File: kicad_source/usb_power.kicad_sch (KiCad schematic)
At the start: 39 parts, among them CN5 USB_C_Receptacle_USB2.0, Q1 2N7002, Q2 2N7002, Q3 BC847, Q4 BC847, Q5 NTR4171P, SW3 SWITCH_INV, U1 TPS383X, U2 MCP73831, U3 TPS736XX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

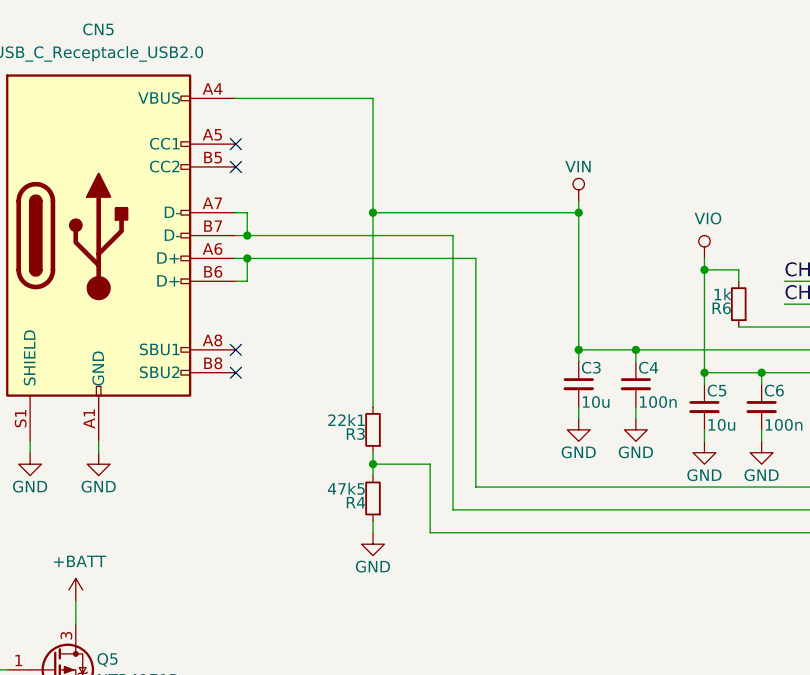
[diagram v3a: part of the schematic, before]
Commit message: added resistors on USB CC
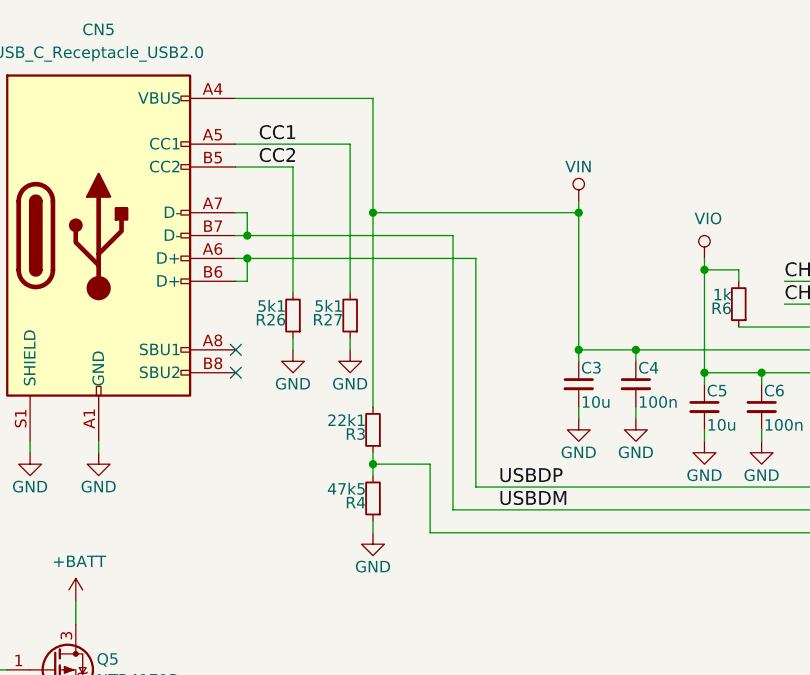
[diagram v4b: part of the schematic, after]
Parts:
- added R26, R27: 5k1, Resistor_SMD:R_0603_1608Metric, symbol Device:R_Small
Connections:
- net GND: now also R26.1, R27.1
- net USBDP: now reaches CN5.A6 (D+), CN5.B6 (D+), U4.4 (D+)
- net USBDM: now reaches CN5.A7 (D-), CN5.B7 (D-), U4.5 (D-)
- net CC1: now reaches CN5.A5 (CC1)
- net CC1: now also R27.2
- net CC2: now reaches CN5.B5 (CC2)
- net CC2: now also R26.2
- no-connect marks 19 -> 17
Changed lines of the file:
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@@
   (title_block
     (title "Sensornator")
-    (date "2022-11-01")
+    (date "2022-11-27")
     (rev "1.2")
     (company "generationmake")
@@
   (no_connect (at 140.97 46.99))
   (no_connect (at 140.97 167.64))
-  (no_connect (at 66.04 39.37))
-  (no_connect (at 66.04 41.91))
   (no_connect (at 66.04 62.23))
   (no_connect (at 66.04 64.77))
@@
     (stroke (width 0) (type default) (color 0 0 0 0))
   )
+  (wire (pts (xy 66.04 39.37) (xy 78.74 39.37))
+    (stroke (width 0) (type default) (color 0 0 0 0))
+  )
   (wire (pts (xy 127 54.61) (xy 140.97 54.61))
     (stroke (width 0) (type default) (color 0 0 0 0))
@@
     (stroke (width 0) (type default) (color 0 0 0 0))
   )
+  (wire (pts (xy 72.39 41.91) (xy 72.39 55.88))
+    (stroke (width 0) (type default) (color 0 0 0 0))
+  )
   (wire (pts (xy 137.16 80.01) (xy 137.16 77.47))
     (stroke (width 0) (type default) (color 0 0 0 0))
@@
     (stroke (width 0) (type default) (color 0 0 0 0))
   )
+  (wire (pts (xy 72.39 60.96) (xy 72.39 62.23))
+    (stroke (width 0) (type default) (color 0 0 0 0))
+  )
   (wire (pts (xy 194.31 46.99) (xy 180.34 46.99))
     (stroke (width 0) (type default) (color 0 0 0 0))
@@
     (stroke (width 0) (type default) (color 0 0 0 0))
   )
+  (wire (pts (xy 78.74 60.96) (xy 78.74 62.23))
+    (stroke (width 0) (type default) (color 0 0 0 0))
+  )
   (wire (pts (xy 67.31 46.99) (xy 67.31 49.53))
     (stroke (width 0) (type default) (color 0 0 0 0))
@@
     (stroke (width 0) (type default) (color 0 0 0 0))
   )
+  (wire (pts (xy 66.04 41.91) (xy 72.39 41.91))
+    (stroke (width 0) (type default) (color 0 0 0 0))
+  )
   (wire (pts (xy 40.64 97.79) (xy 35.56 97.79))
     (stroke (width 0) (type default) (color 0 0 0 0))
@@
     (stroke (width 0) (type default) (color 0 0 0 0))
   )
+  (wire (pts (xy 78.74 39.37) (xy 78.74 55.88))
+    (stroke (width 0) (type default) (color 0 0 0 0))
+  )
   (wire (pts (xy 48.26 110.49) (xy 48.26 102.87))
     (stroke (width 0) (type default) (color 0 0 0 0))
@@
     (effects (font (size 1.524 1.524)) (justify left bottom))
   )
+  (label "USBDP" (at 95.25 77.47 0)
+    (effects (font (size 1.524 1.524)) (justify left bottom))
+  )
   (label "RTS" (at 182.88 52.07 0)
     (effects (font (size 1.524 1.524)) (justify left bottom))
@@
     (effects (font (size 1.524 1.524)) (justify left bottom))
   )
+  (label "CC1" (at 68.58 39.37 0)
+    (effects (font (size 1.524 1.524)) (justify left bottom))
+  )
   (label "BOOT" (at 254 121.92 0)
     (effects (font (size 1.524 1.524)) (justify left bottom))
@@
     (effects (font (size 1.524 1.524)) (justify left bottom))
   )
+  (label "CC2" (at 68.58 41.91 0)
+    (effects (font (size 1.524 1.524)) (justify left bottom))
+  )
   (label "TX" (at 207.01 46.99 0)
+    (effects (font (size 1.524 1.524)) (justify left bottom))
+  )
+  (label "USBDM" (at 95.25 80.01 0)
     (effects (font (size 1.524 1.524)) (justify left bottom))
   )
@@
     (pin "S1")
   )
+  (symbol (lib_id "Device:R_Small") (at 78.74 58.42 180) (unit 1)
+    (in_bom yes) (on_board yes)
+    (property "Reference" "R27" (id 0) (at 77.978 58.928 0)
+      (effects (font (size 1.27 1.27)) (justify left))
+    )
+    (property "Value" "5k1" (id 1) (at 77.978 57.404 0)
+      (effects (font (size 1.27 1.27)) (justify left))
+    )
+    (property "Footprint" "Resistor_SMD:R_0603_1608Metric" (id 2) (at 78.74 54.61 0)
+      (effects (font (size 1.27 1.27)) hide)
+    )
+    (property "Datasheet" "" (id 3) (at 78.74 58.42 0))
+    (pin "1")
+    (pin "2")
+  )
+  (symbol (lib_id "Device:R_Small") (at 72.39 58.42 180) (unit 1)
+    (in_bom yes) (on_board yes)
+    (property "Reference" "R26" (id 0) (at 71.628 58.928 0)
+      (effects (font (size 1.27 1.27)) (justify left))
+    )
+    (property "Value" "5k1" (id 1) (at 71.628 57.404 0)
+      (effects (font (size 1.27 1.27)) (justify left))
+    )
+    (property "Footprint" "Resistor_SMD:R_0603_1608Metric" (id 2) (at 72.39 54.61 0)
+      (effects (font (size 1.27 1.27)) hide)
+    )
+    (property "Datasheet" "" (id 3) (at 72.39 58.42 0))
+    (pin "1")
+    (pin "2")
+  )
+  (symbol (lib_id "power:GND") (at 78.74 62.23 0) (unit 1)
+    (in_bom yes) (on_board yes)
+    (property "Reference" "#PWR037" (id 0) (at 78.74 68.58 0)
+      (effects (font (size 1.27 1.27)) hide)
+    )
+    (property "Value" "GND" (id 1) (at 78.74 66.04 0))
+    (property "Footprint" "" (id 2) (at 78.74 62.23 0))
+    (property "Datasheet" "" (id 3) (at 78.74 62.23 0))
+    (pin "1")
+  )
   (symbol (lib_id "Device:R_Small") (at 251.46 118.11 180) (unit 1)
     (in_bom yes) (on_board yes)
@@
     (pin "1")
   )
+  (symbol (lib_id "power:GND") (at 72.39 62.23 0) (unit 1)
+    (in_bom yes) (on_board yes)
+    (property "Reference" "#PWR035" (id 0) (at 72.39 68.58 0)
+      (effects (font (size 1.27 1.27)) hide)
+    )
+    (property "Value" "GND" (id 1) (at 72.39 66.04 0))
+    (property "Footprint" "" (id 2) (at 72.39 62.23 0))
+    (property "Datasheet" "" (id 3) (at 72.39 62.23 0))
+    (pin "1")
+  )
